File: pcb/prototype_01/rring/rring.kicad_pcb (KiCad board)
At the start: 2 copper layers, 47 x 14.2 mm, 57 parts, among them SW1 Button, U1 DA14531-00000OG2, U2 ADP160ACBZ-1.8-R7, U3 ICM-20948, U4 LTC4124EV-TRMPBF, U5 TCA6418EYFPR, Y1 32MHz

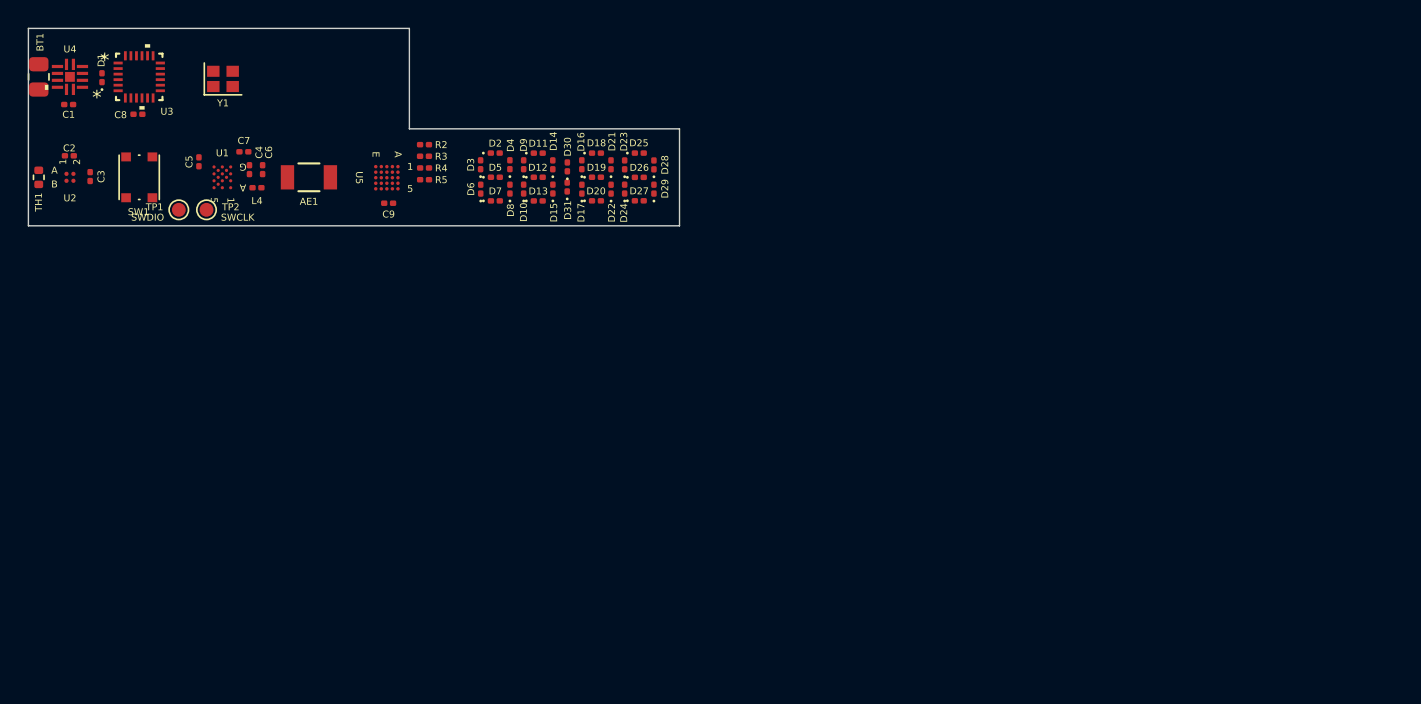
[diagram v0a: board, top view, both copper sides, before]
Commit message: Completed the main PCB of the first prototype
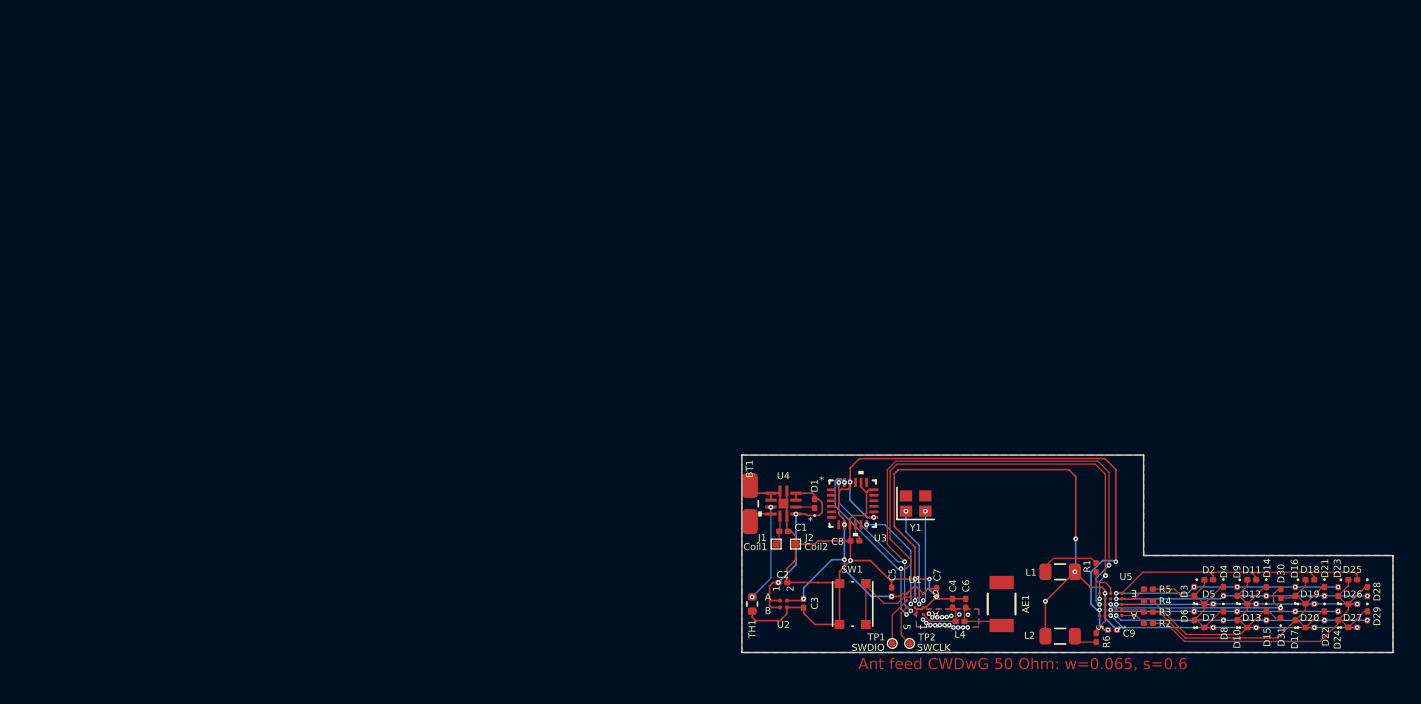
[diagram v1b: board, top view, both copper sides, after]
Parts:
- added J1: Coil1, footprints:Conn_Pad_0.5x0.5mm, F.Cu at (84.0, 60.0)
- added J2: Coil2, footprints:Conn_Pad_0.5x0.5mm, F.Cu at (85.4, 60.0)
- added L1: L, Inductor_SMD:L_0805_2012Metric, F.Cu at (104.5, 62.0)
- added L2: L, Inductor_SMD:L_0805_2012Metric, F.Cu at (104.5, 66.6)
- added R1: 8R, Resistor_SMD:R_0201_0603Metric, F.Cu at (107.1, 61.7)
- added R6: 8R, Resistor_SMD:R_0201_0603Metric, F.Cu at (107.1, 66.7)
- TP1, TP2: footprint TestPoint:TestPoint_Pad_D1.0mm -> footprints:TestPoint_Pad_D0.5mm
- moved R2 62.6 mm to (110.8, 65.7)
- moved R3 61.7 mm to (110.8, 64.9)
- moved R4 60.9 mm to (110.8, 64.1)
- moved C9 60.7 mm to (108.3, 66.2), turned to 0 degrees
- moved U5 60.7 mm to (108.1, 64.3), turned to 180 degrees
- moved TP1 60.3 mm to (92.4, 67.1)
- moved C8 60.2 mm to (89.7, 59.7)
- moved C1 60.1 mm to (84.5, 59.0)
- moved R5 60.0 mm to (110.8, 63.2)
- moved D3 60.0 mm to (114.1, 63.4)
- moved D10 60.0 mm to (117.3, 65.1)
- moved D11 60.0 mm to (118.3, 62.6)
- moved D12 60.0 mm to (118.3, 64.3)
- moved D13 60.0 mm to (118.3, 66.0)
- moved D15 60.0 mm to (119.4, 65.1), turned to -90 degrees
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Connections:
- net Net-(AE1-A) renamed /ANT2
- net Net-(U1-RFIOp) renamed /ANT1
- D23 pad 2: Net-(D10-A) -> Net-(D16-A)
- D24 pad 2: Net-(D16-A) -> Net-(D10-A)
- U5 pad A2: Net-(D16-A) -> Net-(D15-A)
- U5 pad A3: Net-(D15-A) -> Net-(D13-A)
- U5 pad A4: unconnected-(U5-GPIO14-PadA4) -> Net-(U5-GPIO14)
- U5 pad B3: Net-(D13-A) -> Net-(D10-A)
- U5 pad C2: Net-(D14-A) -> Net-(D12-A)
- U5 pad D2: Net-(D12-A) -> Net-(D14-A)
- U5 pad E2: Net-(D10-A) -> Net-(D16-A)
- U5 pad E3: unconnected-(U5-GPIO13-PadE3) -> Net-(U5-GPIO13)
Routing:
- net GND: track 0.00 -> 94.2 mm, vias 0 -> 29
- net +1V8: track 0.00 -> 59.2 mm, vias 0 -> 9
- net SCL: track 0.00 -> 46.2 mm, vias 0 -> 5
- net SDA: track 0.00 -> 45.5 mm, vias 0 -> 5
- net Net-(D23-K): track 0.00 -> 23.3 mm
- net Net-(D16-K): track 0.00 -> 21.3 mm
- net Net-(D11-A): track 0.00 -> 20.1 mm
- net Net-(D15-A): track 0.00 -> 18.3 mm, vias 0 -> 5
- net Net-(D14-A): track 0.00 -> 18.2 mm, vias 0 -> 5
- net Net-(D13-A): track 0.00 -> 18.2 mm, vias 0 -> 5
- net Net-(D10-K): track 0.00 -> 17.9 mm
- net Net-(D12-A): track 0.00 -> 17.4 mm, vias 0 -> 5
- net Net-(D10-A): track 0.00 -> 16.5 mm, vias 0 -> 5
- net Net-(D16-A): track 0.00 -> 16.2 mm, vias 0 -> 5
- net +VDC: track 0.00 -> 14.8 mm, vias 0 -> 2
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- added copper zone on B.Cu, net GND
- added copper zone on F.Cu, net GND
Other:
- outline, holes or cut-outs redrawn
- board text added: "Ant feed CWDwG 50 Ohm: w=0.065, s=0.6"
- board text added: "Vibro Device"
